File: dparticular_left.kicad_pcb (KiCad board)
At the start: 2 copper layers, 185.7 x 157.2 mm, 51 parts, among them J2 Outside USB, J3 To Right Hand, J4 Teensy USB, SW1 Reset, SW1:6 Key_Scrl, SW1:7 Key_Paus, SW2:1 Key_ESC, SW2:2 Key_F1, SW2:3 Key_F2, SW2:4 Key_F3, SW2:5 Key_F4, SW2:6 Key_F5, SW2:7 Key_F6, SW3:1 Key_Home, SW3:2 Key_End, SW3:3 Key_Tilde, SW3:4 Key_1, SW3:5 Key_2, SW3:6 Key_3, SW3:7 Key_4, SW3:8 Key_5, SW4:2 Key_PgUp, SW4:3 Key_Tab, SW4:4 Key_Q, SW4:5 Key_W, SW4:6 Key_E, SW4:7 Key_R, SW4:8 Key_T, SW5:2 Key_PgDn, SW5:3 Key_Caps, SW5:4 Key_A, SW5:5 Key_S, SW5:6 Key_D, SW5:7 Key_F, SW5:8 Key_G, SW6:3 Key_LShft, SW6:4 Key_Z, SW6:5 Key_X, SW6:6 Key_C, SW6:7 Key_V, SW6:8 Key_B, SW7:3 Key_LCtrl, SW7:4 Key_Fn, SW7:5 Key_LWin, SW7:6 Key_LAlt, SW7:8 Key_LSpc, U2 TEENSY2.0

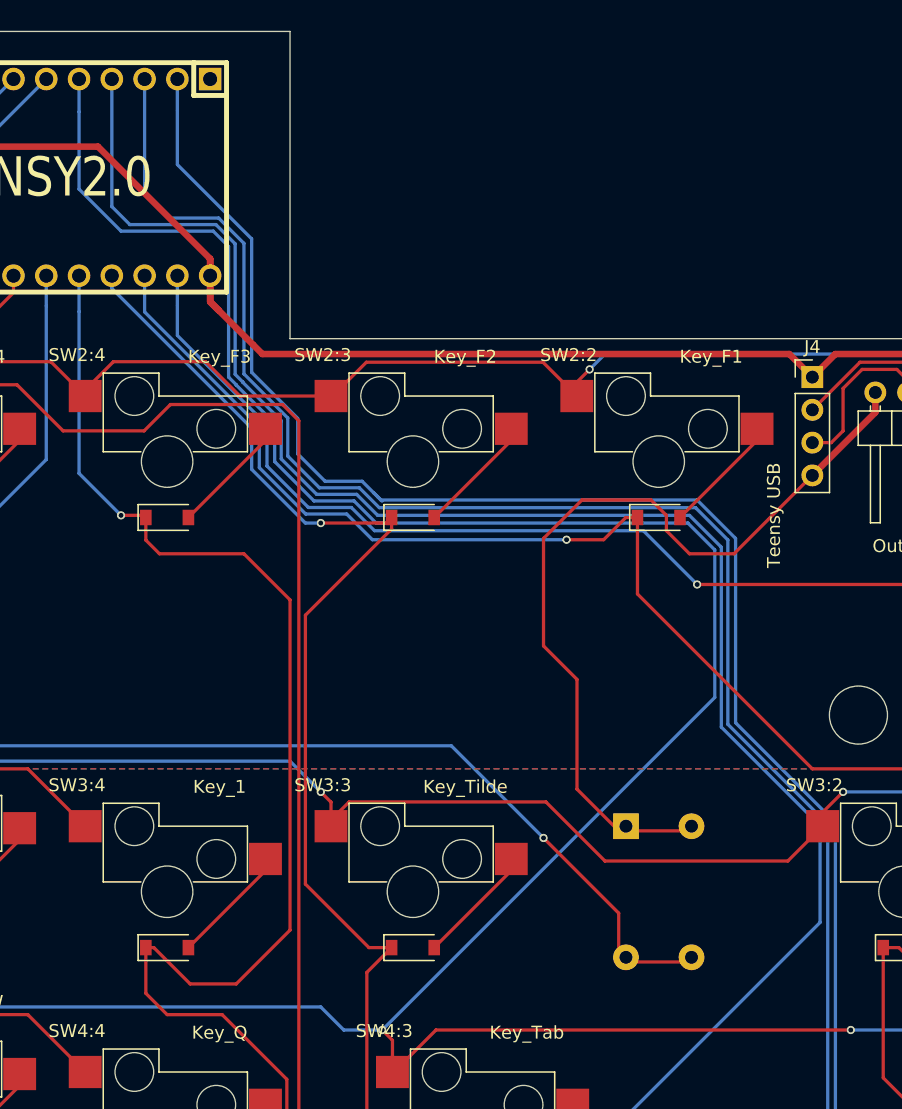
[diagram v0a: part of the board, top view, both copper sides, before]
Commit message: Left Hand PCB: Move traces out from under Reset switch
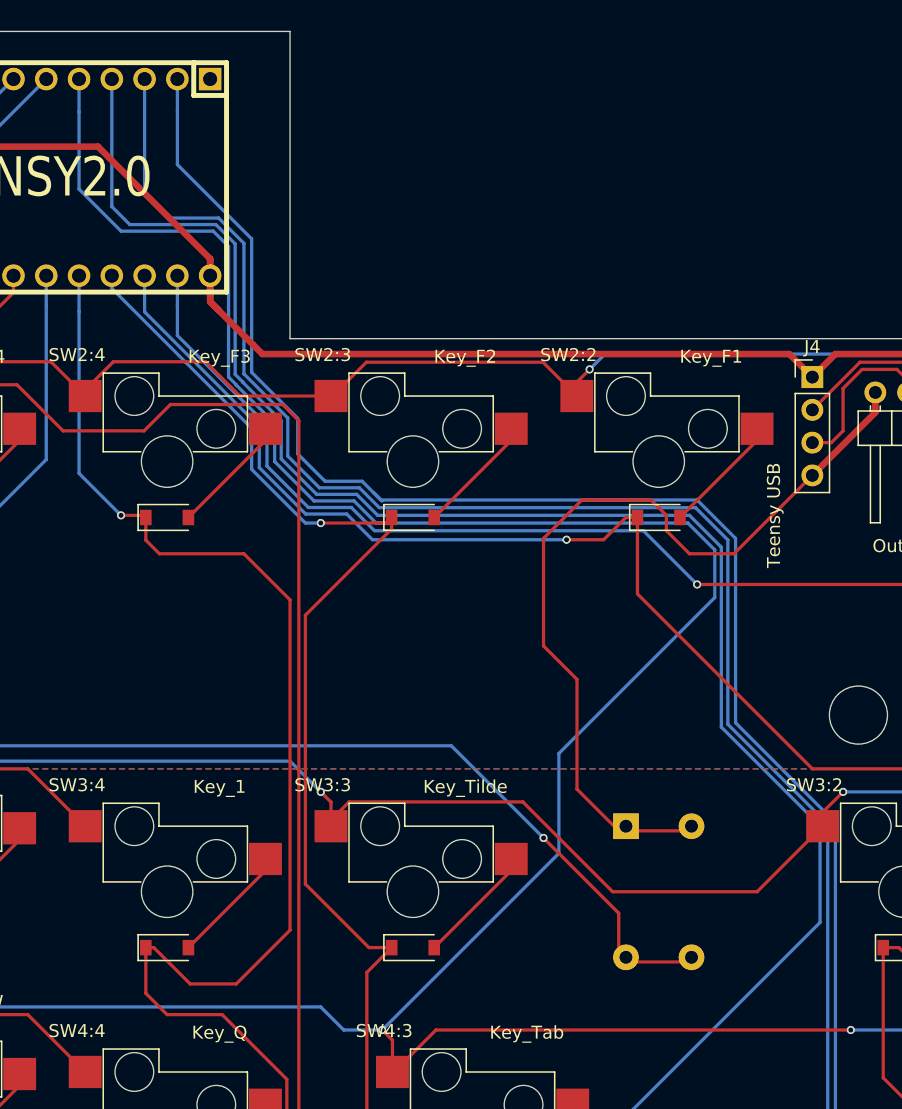
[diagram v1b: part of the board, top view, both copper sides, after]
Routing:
- net /ROW3: track 283.3 -> 285.3 mm

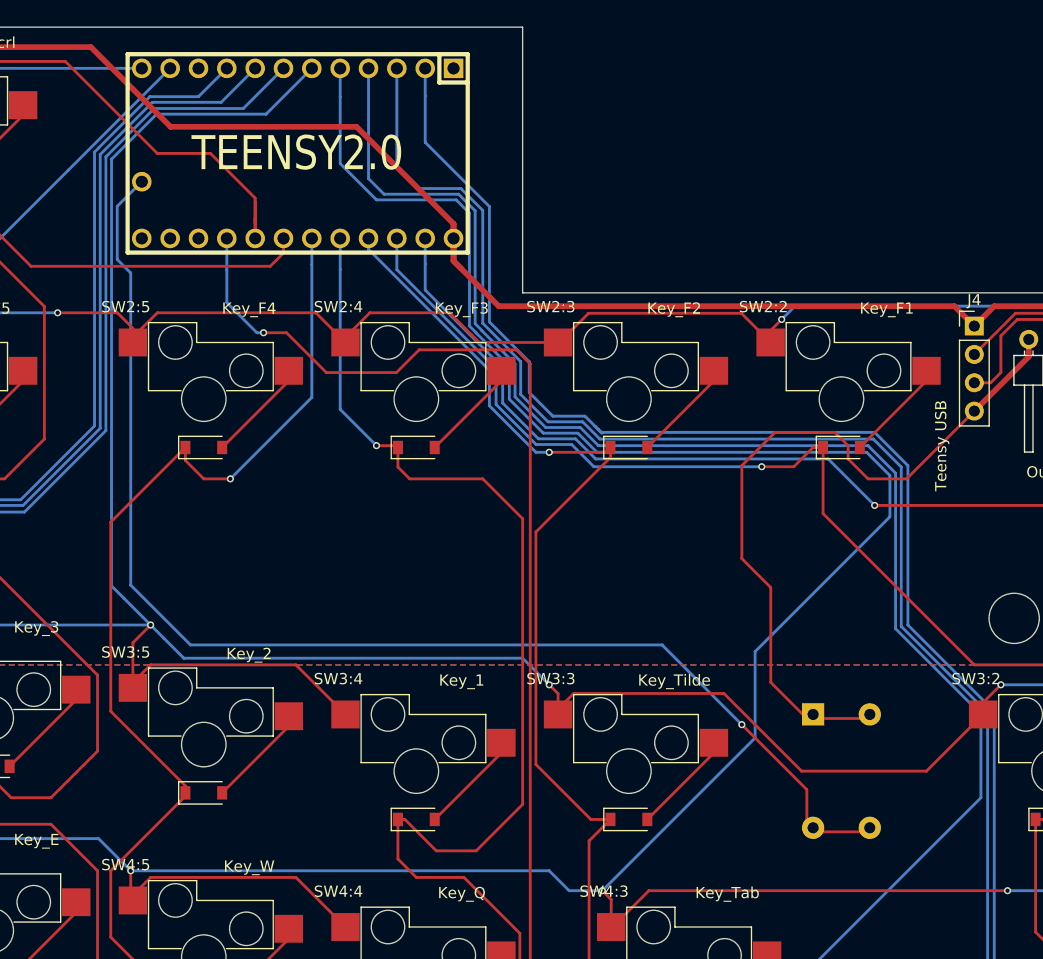
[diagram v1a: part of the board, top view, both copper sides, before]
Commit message: Reset Switch: Use schematic symbol with correct pinout
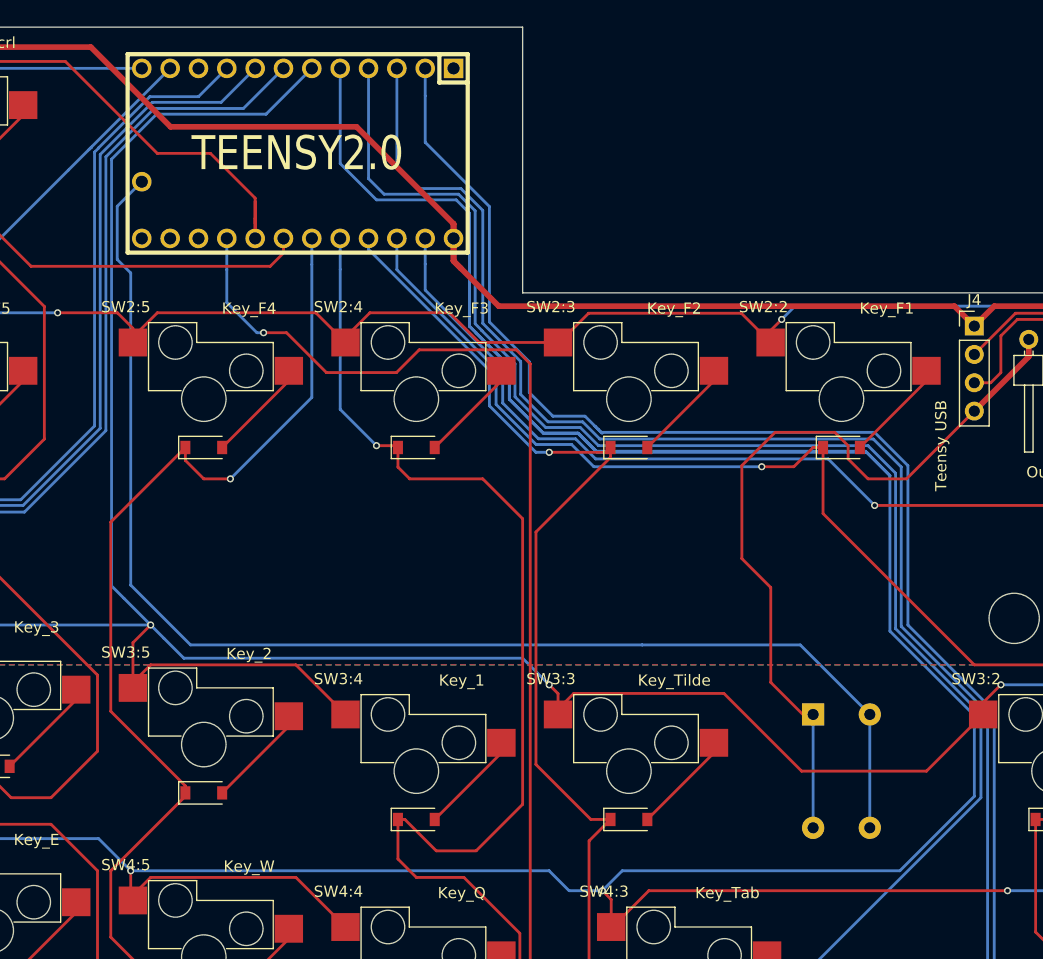
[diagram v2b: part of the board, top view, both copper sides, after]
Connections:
- SW1 pad 2: Net-(SW1-Pad2) -> GND
- SW1 pad 3: GND -> Net-(SW1-Pad3)
- SW1 pad 4: Net-(SW1-Pad2) -> Net-(SW1-Pad3)
- U2 pad 16: Net-(SW1-Pad2) -> Net-(SW1-Pad3)
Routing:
- net Net-(SW1-Pad3): track 0.00 -> 118.8 mm
- net Net-(SW1-Pad2): track 114.6 -> 0.00 mm, vias 1 -> 0
- net /ROW4: track 330.3 -> 432.7 mm
- net GND: track 65.6 -> 70.7 mm

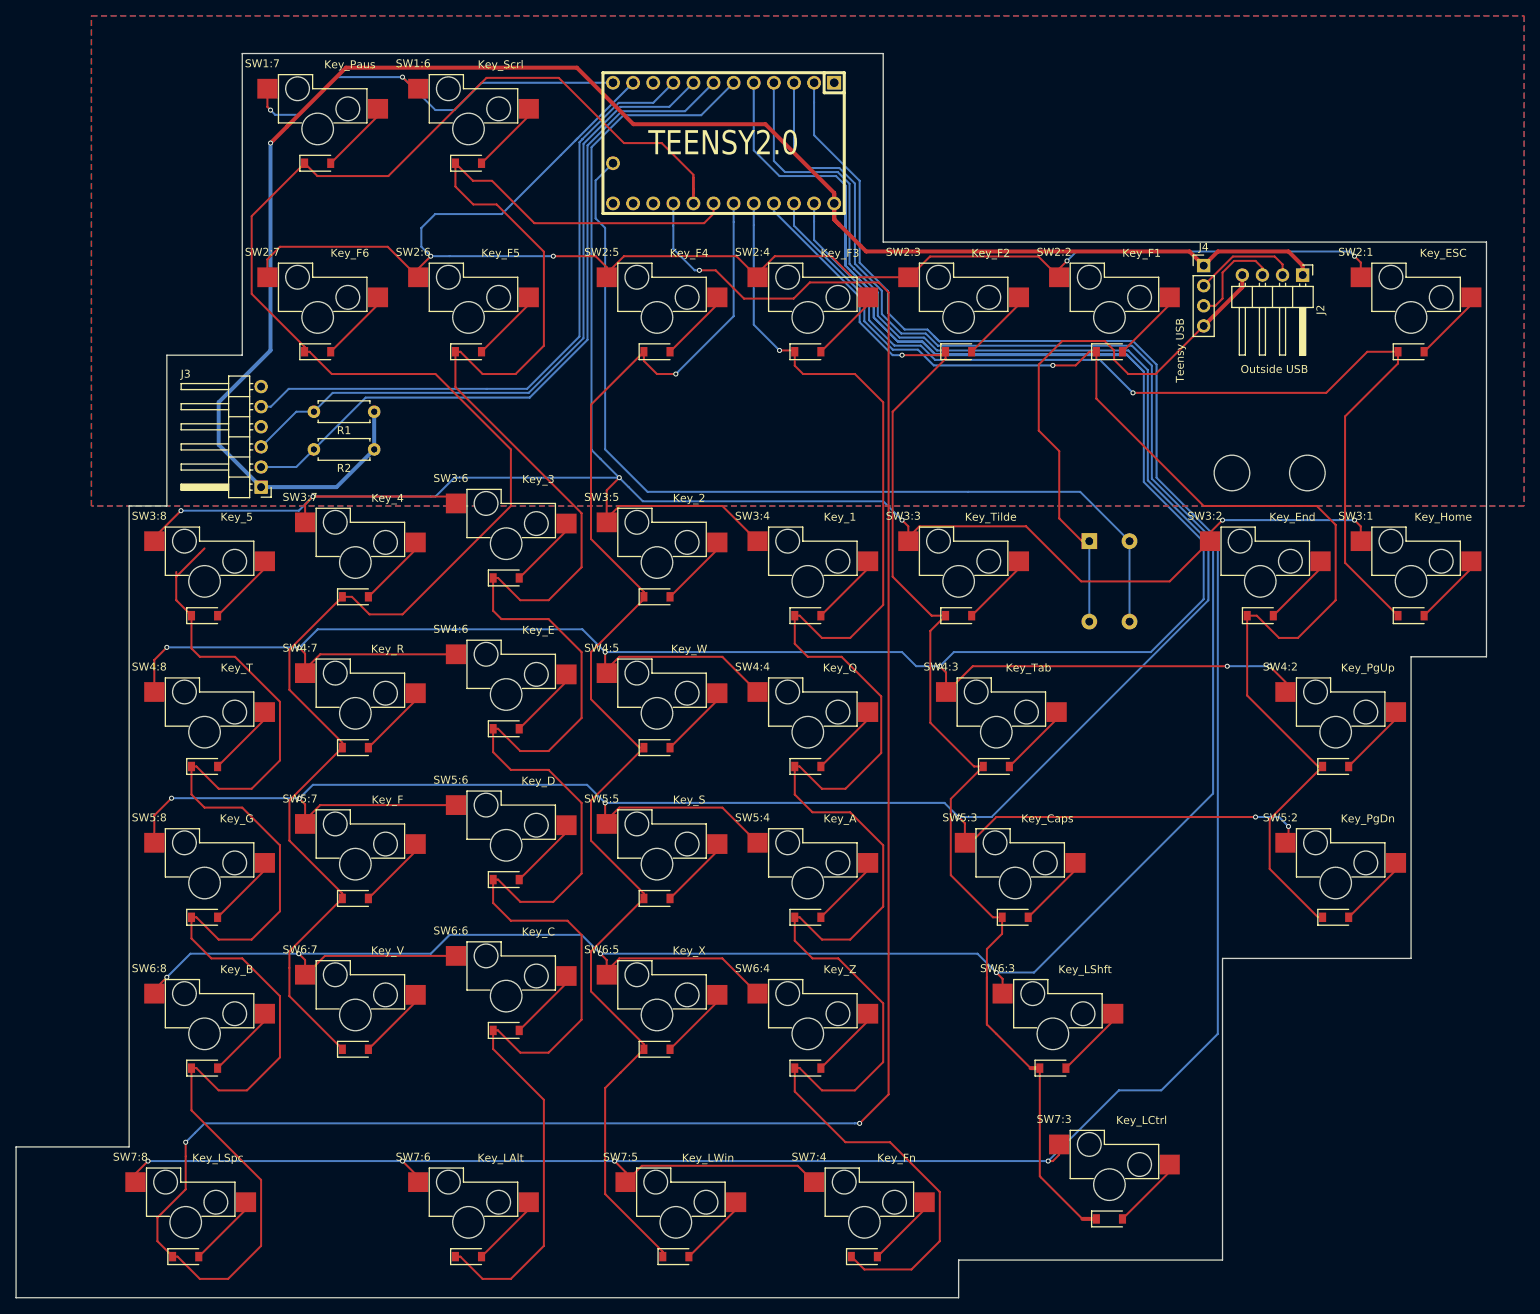
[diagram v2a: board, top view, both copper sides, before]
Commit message: Reset Switch: Move between ESC and F1
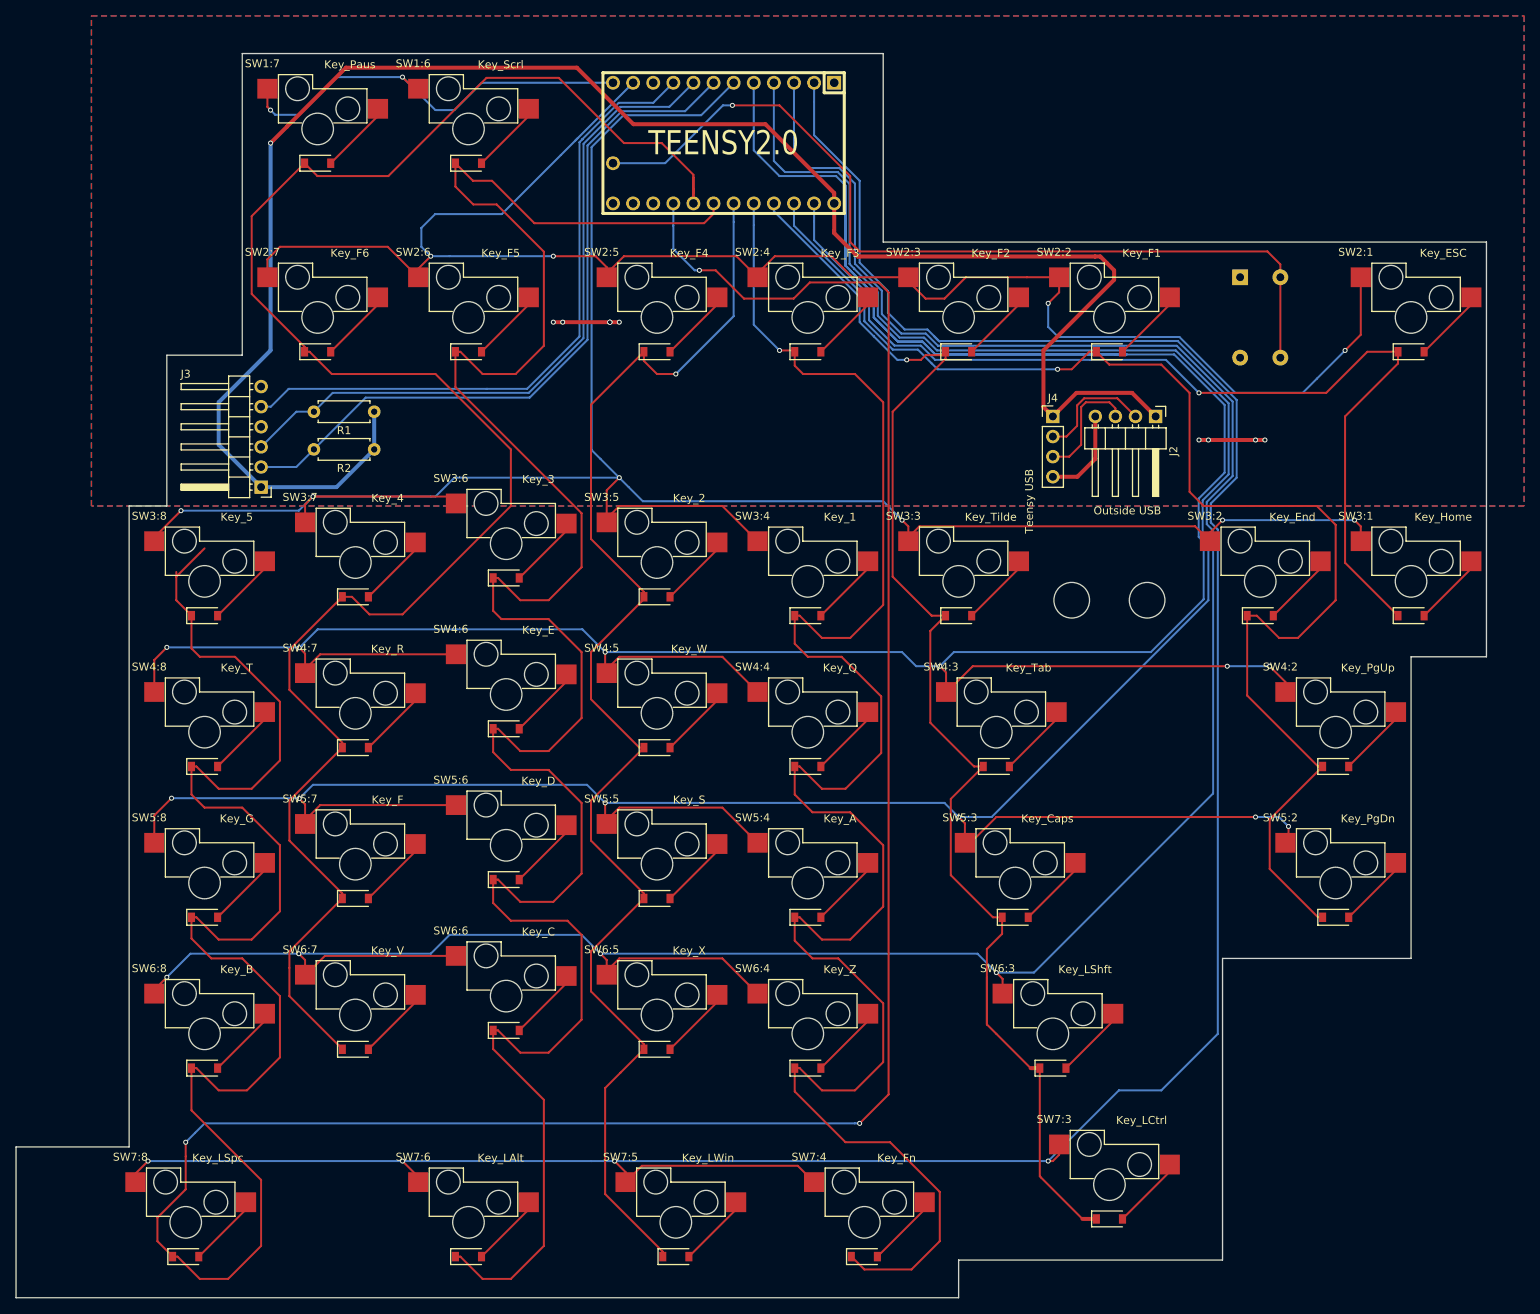
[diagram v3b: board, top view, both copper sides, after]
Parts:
- moved SW1 38.4 mm to (176.2, 57.1)
- moved J4 26.9 mm to (150.0, 69.7)
- moved H1 25.8 mm to (152.4, 92.9)
- moved H2 25.8 mm to (161.9, 92.9)
- moved J2 25.8 mm to (163.0, 69.7)
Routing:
- net GND: track 70.7 -> 28.3 mm, vias 0 -> 9
- net /ROW4: track 432.7 -> 410.8 mm
- net /ROW2: track 196.5 -> 214.4 mm
- net +5V: track 223.0 -> 231.6 mm
- net /ROW5: track 356.4 -> 362.6 mm
- net /ROW7: track 338.6 -> 344.6 mm
- net /ROW6: track 329.6 -> 335.6 mm
- net Net-(SW1-Pad3): track 118.8 -> 113.2 mm, vias 0 -> 1
- net /COL2: track 165.7 -> 170.0 mm
- net /ROW3: track 285.3 -> 281.1 mm
- net /USB_DP: track 13.0 -> 14.9 mm
- net /USB_DN: track 13.3 -> 14.9 mm

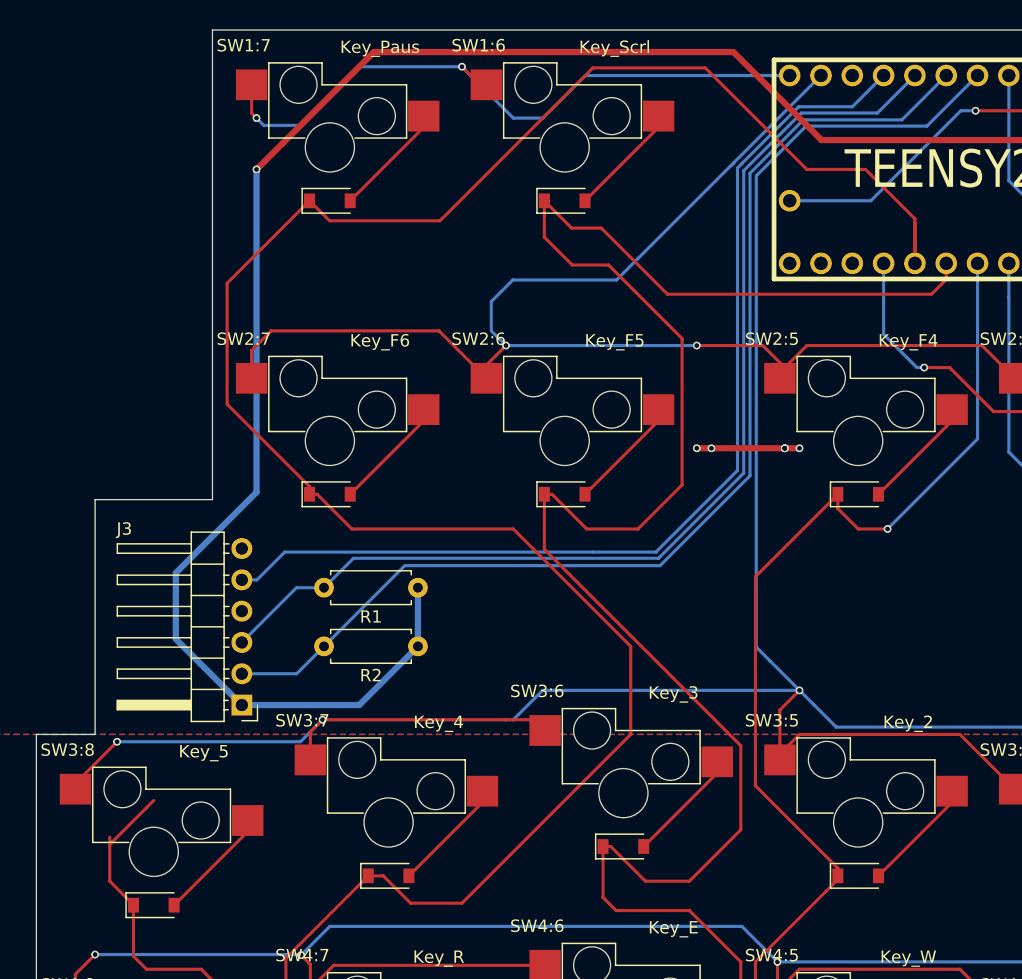
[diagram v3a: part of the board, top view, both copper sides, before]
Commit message: Left Hand PCB: Harmonize inter-board ribbon header orientations
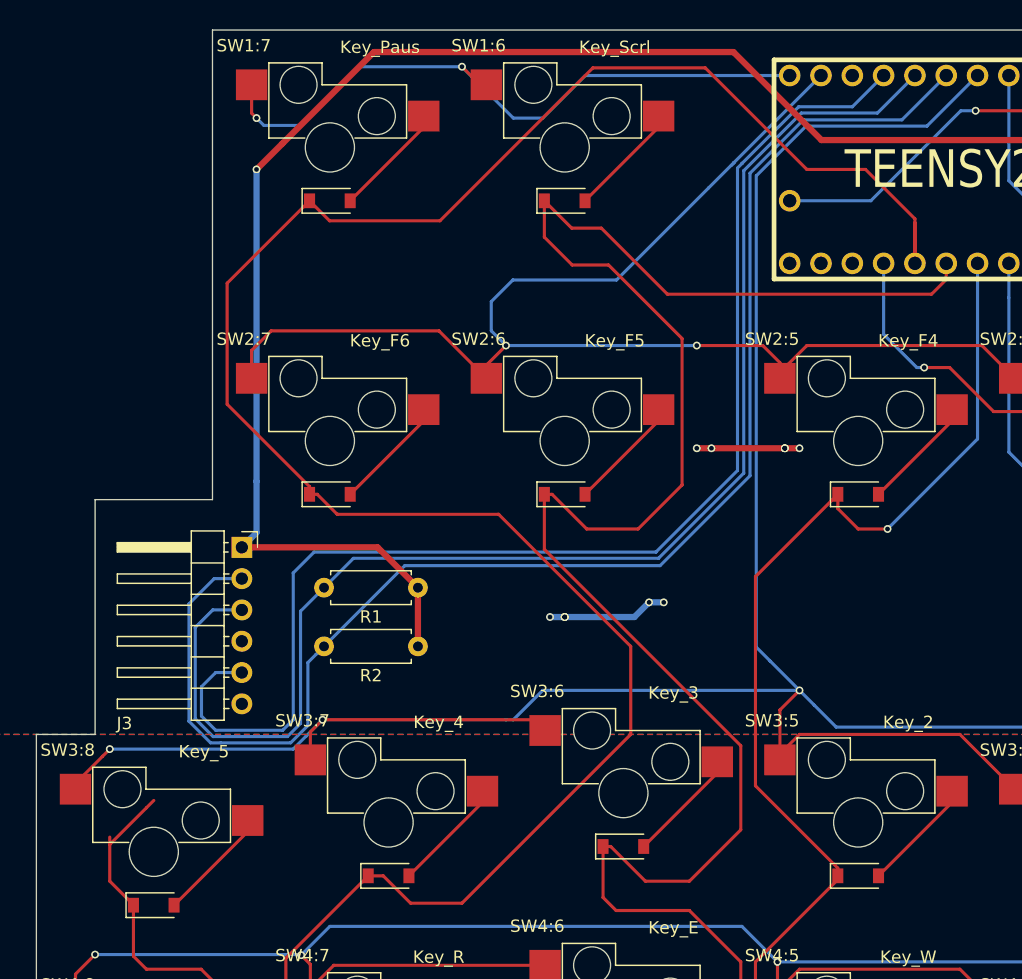
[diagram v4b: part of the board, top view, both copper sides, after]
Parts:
- moved J3 12.8 mm to (50.0, 65.8), turned to 0 degrees
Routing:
- net /SCL: track 91.6 -> 116.6 mm
- net /SDA: track 88.0 -> 112.7 mm
- net /LED_D: track 83.4 -> 105.3 mm
- net +5V: track 231.6 -> 213.7 mm
- net GND: track 28.3 -> 38.0 mm, vias 9 -> 14
